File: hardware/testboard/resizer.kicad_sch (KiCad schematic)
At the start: 2 parts

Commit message: work on testboard
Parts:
- added R21, R22: 1k, symbol Device:R_Small_US
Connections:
- net +5V: now also R21.1, R22.1
- net ~{DSACK0}: now also R22.2
- net ~{DSACK1}: now also R21.2
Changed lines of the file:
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@@
 (kicad_sch (version 20230121) (generator eeschema)
   (paper "A4")
+  (junction (at 160.02 139.7) (diameter 0) (color 0 0 0 0)
+  )
   (junction (at 109.22 43.18) (diameter 0) (color 0 0 0 0)
   )
+  (junction (at 154.94 137.16) (diameter 0) (color 0 0 0 0)
+  )
+  (junction (at 160.02 129.54) (diameter 0) (color 0 0 0 0)
+  )
   (bus_entry (at 88.9 101.6) (size -2.54 -2.54)
     (stroke (width 0) (type default))
@@
     (stroke (width 0) (type default))
   )
-  (bus_entry (at 144.78 139.7) (size 2.54 -2.54)
+  (bus_entry (at 167.64 139.7) (size 2.54 -2.54)
     (stroke (width 0) (type default))
   )
@@
     (stroke (width 0) (type default))
   )
-  (bus_entry (at 144.78 137.16) (size 2.54 -2.54)
+  (bus_entry (at 167.64 137.16) (size 2.54 -2.54)
     (stroke (width 0) (type default))
   )
@@
     (stroke (width 0) (type default))
   )
+  (wire (pts (xy 154.94 134.62) (xy 154.94 137.16))
+    (stroke (width 0) (type default))
+  )
   (bus (pts (xy 137.16 116.84) (xy 137.16 114.3))
     (stroke (width 0) (type default))
@@
     (stroke (width 0) (type default))
   )
+  (wire (pts (xy 154.94 129.54) (xy 160.02 129.54))
+    (stroke (width 0) (type default))
+  )
   (wire (pts (xy 93.98 106.68) (xy 88.9 106.68))
     (stroke (width 0) (type default))
   )
-  (wire (pts (xy 127 137.16) (xy 144.78 137.16))
+  (wire (pts (xy 127 137.16) (xy 154.94 137.16))
     (stroke (width 0) (type default))
   )
@@
     (stroke (width 0) (type default))
   )
-  (bus (pts (xy 147.32 134.62) (xy 147.32 137.16))
+  (bus (pts (xy 170.18 134.62) (xy 170.18 137.16))
     (stroke (width 0) (type default))
   )
@@
     (stroke (width 0) (type default))
   )
+  (wire (pts (xy 160.02 134.62) (xy 160.02 139.7))
+    (stroke (width 0) (type default))
+  )
   (wire (pts (xy 93.98 99.06) (xy 88.9 99.06))
     (stroke (width 0) (type default))
@@
     (stroke (width 0) (type default))
   )
+  (wire (pts (xy 154.94 137.16) (xy 167.64 137.16))
+    (stroke (width 0) (type default))
+  )
   (wire (pts (xy 127 104.14) (xy 134.62 104.14))
     (stroke (width 0) (type default))
   )
+  (wire (pts (xy 160.02 139.7) (xy 167.64 139.7))
+    (stroke (width 0) (type default))
+  )
   (wire (pts (xy 76.2 134.62) (xy 93.98 134.62))
     (stroke (width 0) (type default))
@@
     (stroke (width 0) (type default))
   )
-  (bus (pts (xy 147.32 134.62) (xy 154.94 134.62))
+  (bus (pts (xy 170.18 134.62) (xy 177.8 134.62))
     (stroke (width 0) (type default))
   )
@@
     (stroke (width 0) (type default))
   )
-  (wire (pts (xy 127 139.7) (xy 144.78 139.7))
+  (wire (pts (xy 127 139.7) (xy 160.02 139.7))
     (stroke (width 0) (type default))
   )
@@
     (effects (font (size 1.27 1.27)) (justify right))
   )
-  (hierarchical_label "~{DSACK[0..1]}" (shape input) (at 154.94 134.62 0) (fields_autoplaced)
+  (hierarchical_label "~{DSACK[0..1]}" (shape input) (at 177.8 134.62 0) (fields_autoplaced)
     (effects (font (size 1.27 1.27)) (justify left))
   )
@@
         (path "/a1ce156a-fb78-423b-b05a-d07384e5c8a7/996cf3c7-017a-4ebb-baec-dabb3d5e06f2"
           (reference "#PWR014") (unit 1)
+        )
+      )
+    )
+  )
+  (symbol (lib_id "Device:R_Small_US") (at 160.02 132.08 0) (unit 1)
+    (in_bom yes) (on_board yes) (dnp no) (fields_autoplaced)
+    (property "Reference" "R22" (at 162.56 130.81 0)
+      (effects (font (size 1.27 1.27)) (justify left))
+    )
+    (property "Value" "1k" (at 162.56 133.35 0)
+      (effects (font (size 1.27 1.27)) (justify left))
+    )
+    (property "Footprint" "" (at 160.02 132.08 0)
+      (effects (font (size 1.27 1.27)) hide)
+    )
+    (property "Datasheet" "~" (at 160.02 132.08 0)
+      (effects (font (size 1.27 1.27)) hide)
+    )
+    (pin "1")
+    (pin "2")
+    (instances
+      (project "testboard"
+        (path "/a1ce156a-fb78-423b-b05a-d07384e5c8a7/996cf3c7-017a-4ebb-baec-dabb3d5e06f2"
+          (reference "R22") (unit 1)
         )
       )
@@
     )
   )
+  (symbol (lib_id "Device:R_Small_US") (at 154.94 132.08 0) (mirror y) (unit 1)
+    (in_bom yes) (on_board yes) (dnp no)
+    (property "Reference" "R21" (at 152.4 130.81 0)
+      (effects (font (size 1.27 1.27)) (justify left))
+    )
+    (property "Value" "1k" (at 152.4 133.35 0)
+      (effects (font (size 1.27 1.27)) (justify left))
+    )
+    (property "Footprint" "" (at 154.94 132.08 0)
+      (effects (font (size 1.27 1.27)) hide)
+    )
+    (property "Datasheet" "~" (at 154.94 132.08 0)
+      (effects (font (size 1.27 1.27)) hide)
+    )
+    (pin "1")
+    (pin "2")
+    (instances
+      (project "testboard"
+        (path "/a1ce156a-fb78-423b-b05a-d07384e5c8a7/996cf3c7-017a-4ebb-baec-dabb3d5e06f2"
+          (reference "R21") (unit 1)
+        )
+      )
+    )
+  )
   (symbol (lib_id "Device:C") (at 132.08 46.99 0) (unit 1)
     (in_bom yes) (on_board yes) (dnp no) (fields_autoplaced)
@@
         )
       )
+    )
+  )
+  (symbol (lib_id "power:+5V") (at 160.02 129.54 0) (unit 1)
+    (in_bom yes) (on_board yes) (dnp no) (fields_autoplaced)
+    (property "Reference" "#PWR0124" (at 160.02 133.35 0)
+      (effects (font (size 1.27 1.27)) hide)
+    )
+    (property "Value" "+5V" (at 160.02 124.46 0)
+      (effects (font (size 1.27 1.27)))
+    )
+    (property "Footprint" "" (at 160.02 129.54 0)
+      (effects (font (size 1.27 1.27)) hide)
+    )
+    (property "Datasheet" "" (at 160.02 129.54 0)
+      (effects (font (size 1.27 1.27)) hide)
+    )
+    (pin "1")
+    (instances
+      (project "testboard"
+        (path "/a1ce156a-fb78-423b-b05a-d07384e5c8a7/996cf3c7-017a-4ebb-baec-dabb3d5e06f2"
+          (reference "#PWR0124") (unit 1)
+        )
+      )

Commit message: simpleboard nearly complete
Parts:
- C27: value .1uF -> 100nF; footprint (none) -> Capacitor_SMD:C_0603_1608Metric
- R21, R22: footprint (none) -> Resistor_SMD:R_0603_1608Metric
- U9: footprint Package_LCC:PLCC-68_SMD-Socket -> Package_LCC:PLCC-68_THT-Socket
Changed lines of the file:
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@@
       (effects (font (size 1.27 1.27)) (justify left))
     )
-    (property "Footprint" "" (at 160.02 132.08 0)
+    (property "Footprint" "Resistor_SMD:R_0603_1608Metric" (at 160.02 132.08 0)
       (effects (font (size 1.27 1.27)) hide)
     )
@@
       (effects (font (size 1.27 1.27)))
     )
-    (property "Footprint" "Package_LCC:PLCC-68_SMD-Socket" (at 124.46 83.82 0)
+    (property "Footprint" "Package_LCC:PLCC-68_THT-Socket" (at 124.46 83.82 0)
       (effects (font (size 1.27 1.27)) hide)
     )
@@
       (effects (font (size 1.27 1.27)) (justify left))
     )
-    (property "Footprint" "" (at 154.94 132.08 0)
+    (property "Footprint" "Resistor_SMD:R_0603_1608Metric" (at 154.94 132.08 0)
       (effects (font (size 1.27 1.27)) hide)
     )
@@
       (effects (font (size 1.27 1.27)) (justify left))
     )
-    (property "Value" ".1uF" (at 135.89 48.26 0)
+    (property "Value" "100nF" (at 135.89 48.26 0)
       (effects (font (size 1.27 1.27)) (justify left))
     )
-    (property "Footprint" "" (at 133.0452 50.8 0)
+    (property "Footprint" "Capacitor_SMD:C_0603_1608Metric" (at 133.0452 50.8 0)
       (effects (font (size 1.27 1.27)) hide)
     )

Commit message: pinouts
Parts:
- renumbered C27 to C601, R21 to R601, R22 to R602, U9 to U601
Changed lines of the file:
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@@
   (symbol (lib_id "power:GND") (at 109.22 157.48 0) (unit 1)
     (in_bom yes) (on_board yes) (dnp no) (fields_autoplaced)
-    (property "Reference" "#PWR014" (at 109.22 163.83 0)
+    (property "Reference" "#PWR0602" (at 109.22 163.83 0)
       (effects (font (size 1.27 1.27)) hide)
     )
@@
       (project "testboard"
         (path "/a1ce156a-fb78-423b-b05a-d07384e5c8a7/996cf3c7-017a-4ebb-baec-dabb3d5e06f2"
-          (reference "#PWR014") (unit 1)
+          (reference "#PWR0602") (unit 1)
         )
       )
@@
   (symbol (lib_id "Device:R_Small_US") (at 160.02 132.08 0) (unit 1)
     (in_bom yes) (on_board yes) (dnp no) (fields_autoplaced)
-    (property "Reference" "R22" (at 162.56 130.81 0)
+    (property "Reference" "R602" (at 162.56 130.81 0)
       (effects (font (size 1.27 1.27)) (justify left))
     )
@@
       (project "testboard"
         (path "/a1ce156a-fb78-423b-b05a-d07384e5c8a7/996cf3c7-017a-4ebb-baec-dabb3d5e06f2"
-          (reference "R22") (unit 1)
+          (reference "R602") (unit 1)
         )
       )
@@
   (symbol (lib_id "power:GND") (at 132.08 50.8 0) (unit 1)
     (in_bom yes) (on_board yes) (dnp no) (fields_autoplaced)
-    (property "Reference" "#PWR013" (at 132.08 57.15 0)
+    (property "Reference" "#PWR0603" (at 132.08 57.15 0)
       (effects (font (size 1.27 1.27)) hide)
     )
@@
       (project "testboard"
         (path "/a1ce156a-fb78-423b-b05a-d07384e5c8a7/996cf3c7-017a-4ebb-baec-dabb3d5e06f2"
-          (reference "#PWR013") (unit 1)
+          (reference "#PWR0603") (unit 1)
         )
       )
@@
   (symbol (lib_id "power:+5V") (at 109.22 43.18 0) (unit 1)
     (in_bom yes) (on_board yes) (dnp no) (fields_autoplaced)
-    (property "Reference" "#PWR012" (at 109.22 46.99 0)
+    (property "Reference" "#PWR0601" (at 109.22 46.99 0)
       (effects (font (size 1.27 1.27)) hide)
     )
@@
       (project "testboard"
         (path "/a1ce156a-fb78-423b-b05a-d07384e5c8a7/996cf3c7-017a-4ebb-baec-dabb3d5e06f2"
-          (reference "#PWR012") (unit 1)
+          (reference "#PWR0601") (unit 1)
         )
       )
@@
   (symbol (lib_id "68040:MC68150") (at 109.22 104.14 0) (unit 1)
     (in_bom yes) (on_board yes) (dnp no) (fields_autoplaced)
-    (property "Reference" "U9" (at 111.4141 43.18 0)
+    (property "Reference" "U601" (at 111.4141 43.18 0)
       (effects (font (size 1.27 1.27)) (justify left))
     )
@@
       (project "testboard"
         (path "/a1ce156a-fb78-423b-b05a-d07384e5c8a7/996cf3c7-017a-4ebb-baec-dabb3d5e06f2"
-          (reference "U9") (unit 1)
+          (reference "U601") (unit 1)
         )
       )
@@
   (symbol (lib_id "Device:R_Small_US") (at 154.94 132.08 0) (mirror y) (unit 1)
     (in_bom yes) (on_board yes) (dnp no)
-    (property "Reference" "R21" (at 152.4 130.81 0)
+    (property "Reference" "R601" (at 152.4 130.81 0)
       (effects (font (size 1.27 1.27)) (justify left))
     )
@@
       (project "testboard"
         (path "/a1ce156a-fb78-423b-b05a-d07384e5c8a7/996cf3c7-017a-4ebb-baec-dabb3d5e06f2"
-          (reference "R21") (unit 1)
+          (reference "R601") (unit 1)
         )
       )
@@
   (symbol (lib_id "Device:C") (at 132.08 46.99 0) (unit 1)
     (in_bom yes) (on_board yes) (dnp no) (fields_autoplaced)
-    (property "Reference" "C27" (at 135.89 45.72 0)
+    (property "Reference" "C601" (at 135.89 45.72 0)
       (effects (font (size 1.27 1.27)) (justify left))
     )
@@
       (project "testboard"
         (path "/a1ce156a-fb78-423b-b05a-d07384e5c8a7/996cf3c7-017a-4ebb-baec-dabb3d5e06f2"
-          (reference "C27") (unit 1)
+          (reference "C601") (unit 1)
         )
       )
@@
   (symbol (lib_id "power:+5V") (at 160.02 129.54 0) (unit 1)
     (in_bom yes) (on_board yes) (dnp no) (fields_autoplaced)
-    (property "Reference" "#PWR0124" (at 160.02 133.35 0)
+    (property "Reference" "#PWR0604" (at 160.02 133.35 0)
       (effects (font (size 1.27 1.27)) hide)
     )
@@
       (project "testboard"
         (path "/a1ce156a-fb78-423b-b05a-d07384e5c8a7/996cf3c7-017a-4ebb-baec-dabb3d5e06f2"
-          (reference "#PWR0124") (unit 1)
-        )
-      )
+          (reference "#PWR0604") (unit 1)
+        )
+      )

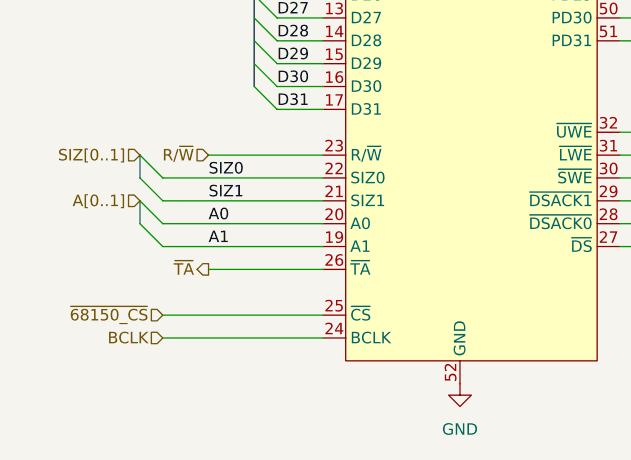
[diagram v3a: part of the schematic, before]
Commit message: update errata for testboard
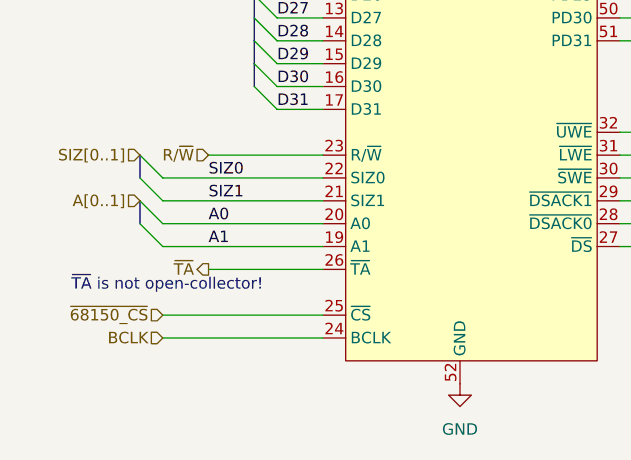
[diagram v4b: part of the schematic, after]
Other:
- note added: "~{TA} is not open-collector!"
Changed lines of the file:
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@@
     (stroke (width 0) (type default))
+  )
+  (text "~{TA} is not open-collector!" (at 66.04 147.32 0)
+    (effects (font (size 1.27 1.27)) (justify left bottom))
   )
   (label "D4" (at 88.9 58.42 0) (fields_autoplaced)
